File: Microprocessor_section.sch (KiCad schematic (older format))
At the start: 14 parts, among them J15 Conn_01x06_Male, SW1 K2-1102SP-C4SC-04, U5 ESP32-WROOM-32D

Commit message: Start PCB layout
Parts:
- removed SW1: K2-1102SP-C4SC-04, co2_sensor_node:K2-1102SP-xxxC, symbol Switch:SW_MEC_5G
- added SW1: K2-1102SP-C4SC-04, co2_sensor_node:K2-1102SP-xxxC, symbol Switch:SW_Push
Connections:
- net EN: now also SW1.2
- net GND: now also SW1.1
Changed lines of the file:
@@
 Text HLabel 7600 3500 2    50   Output ~ 0
 UART1_TX
-$Comp
-L Switch:SW_MEC_5G SW1
-U 1 1 60A91701
-P 5200 3050
-F 0 "SW1" V 5150 3300 50  0000 R CNN
-F 1 "K2-1102SP-C4SC-04" V 5250 3150 50  0000 L CNN
-F 2 "co2_sensor_node:K2-1102SP-xxxC" H 5200 3250 50  0001 C CNN
-F 3 "https://datasheet.lcsc.com/szlcsc/1811082113_Korean-Hroparts-Elec-K2-1102SP-C4SC-04_C127509.pdf" H 5200 3250 50  0001 C CNN
-F 4 "https://lcsc.com/product-detail/Tactile-Switches_Korean-Hroparts-Elec-K2-1102SP-C4SC-04_C127509.html/?href=jlc-SMT" V 5200 3050 50  0001 C CNN "LCSC"
-	1    5200 3050
-	0    -1   1    0
-$EndComp
 Wire Wire Line
 	5200 2800 5200 2850
@@
 Wire Wire Line
 	2300 4100 2600 4100
+$Comp
+L Switch:SW_Push SW1
+U 1 1 60B19388
+P 5200 3050
+F 0 "SW1" V 5246 3150 50  0000 L CNN
+F 1 "K2-1102SP-C4SC-04" V 5118 3150 50  0000 L CNN
+F 2 "co2_sensor_node:K2-1102SP-xxxC" H 5200 3250 50  0001 C CNN
+F 3 "https://datasheet.lcsc.com/szlcsc/1811082113_Korean-Hroparts-Elec-K2-1102SP-C4SC-04_C127509.pdf" H 5200 3250 50  0001 C CNN
+F 4 "https://lcsc.com/product-detail/Tactile-Switches_Korean-Hroparts-Elec-K2-1102SP-C4SC-04_C127509.html/?href=jlc-SMT" V 5200 3050 50  0001 C CNN "LCSC"
+	1    5200 3050
+	0    -1   -1   0
+$EndComp
 $EndSCHEMATC

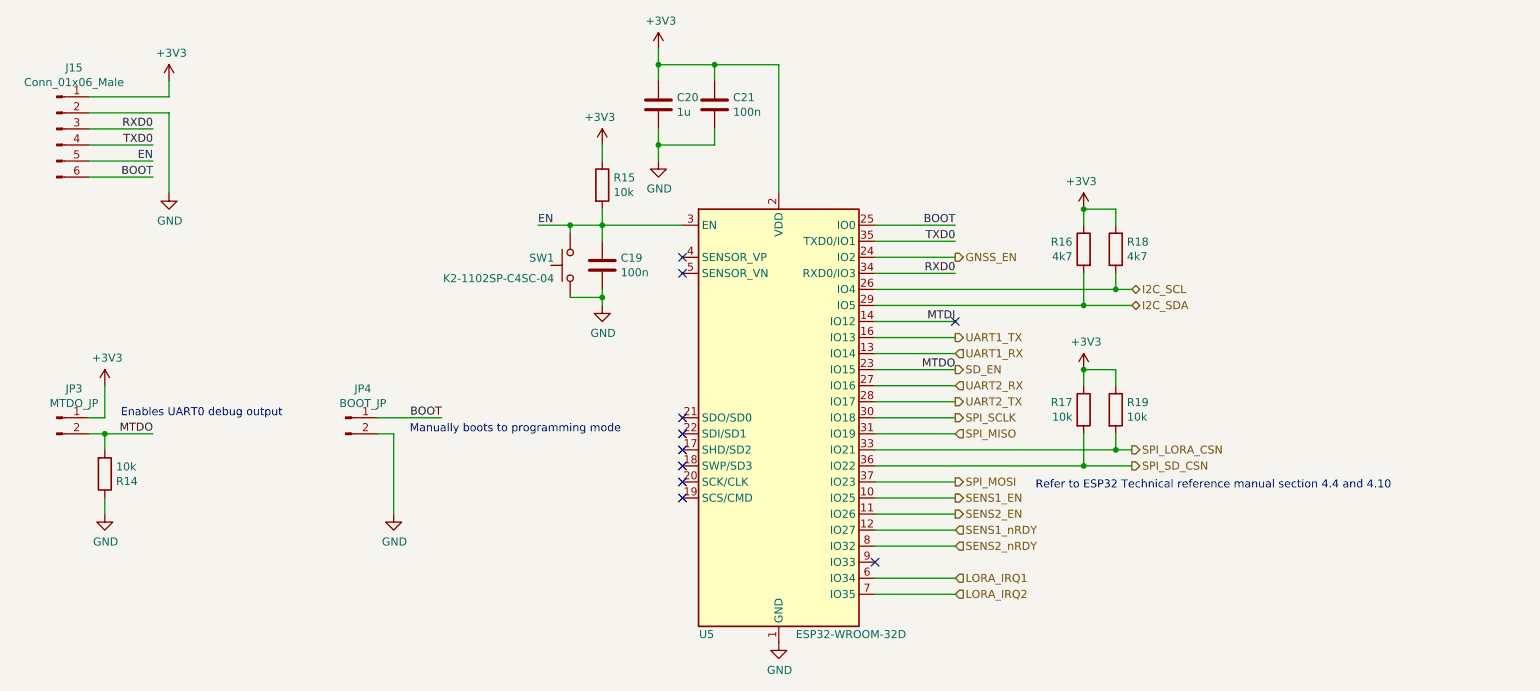
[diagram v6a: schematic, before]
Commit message: First cut at layout
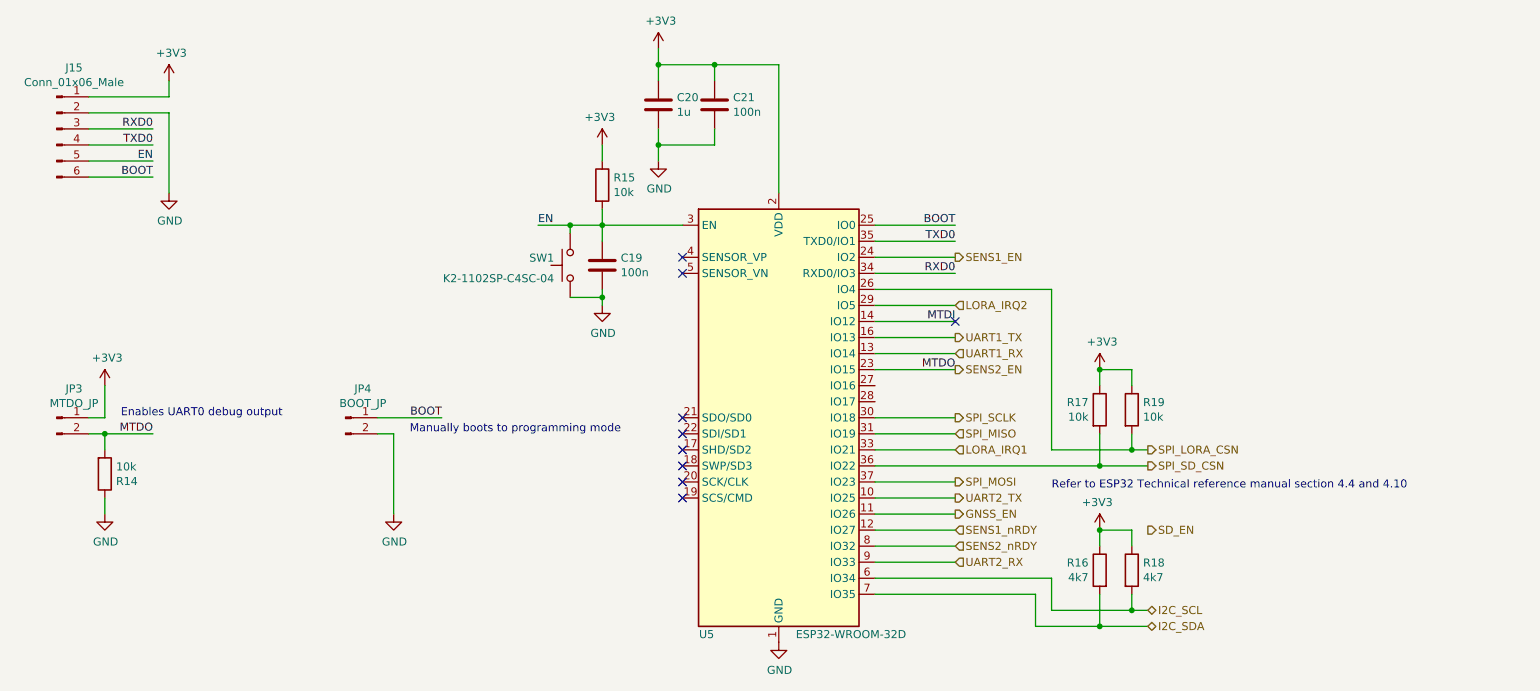
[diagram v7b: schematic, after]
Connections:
- net GNSS_EN: now also U5.11 (IO26); no longer U5.24 (IO2)
- net I2C_SCL: now also U5.6 (IO34); no longer U5.26 (IO4)
- net I2C_SDA: now also U5.7 (IO35); no longer U5.29 (IO5)
- net LORA_IRQ1: now also U5.33 (IO21); no longer U5.6 (IO34)
- net LORA_IRQ2: now also U5.29 (IO5); no longer U5.7 (IO35)
- net SD_EN: no longer JP3.2 (Pin_2), R14.2, U5.23 (IO15)
- net SENS1_EN: now also U5.24 (IO2); no longer U5.10 (IO25)
- net SENS2_EN: now also JP3.2 (Pin_2), R14.2, U5.23 (IO15); no longer U5.11 (IO26)
- net SPI_LORA_CSN: now also U5.26 (IO4); no longer U5.33 (IO21)
- net UART2_RX: now also U5.9 (IO33); no longer U5.27 (IO16)
- net UART2_TX: now also U5.10 (IO25); no longer U5.28 (IO17)
- no-connect marks 10 -> 9
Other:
- moved on the sheet: R16, R17, R18, R19
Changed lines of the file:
@@
 $EndComp
 Wire Wire Line
-	7100 3200 8600 3200
-Wire Wire Line
-	8400 3100 8400 3300
-Wire Wire Line
-	8400 3300 8700 3300
-Connection ~ 8400 3300
-Wire Wire Line
-	7100 3300 8400 3300
-Connection ~ 8400 2700
-Wire Wire Line
-	8600 4200 8700 4200
-Connection ~ 8600 4200
-Wire Wire Line
-	8600 4100 8600 4200
-Wire Wire Line
-	8400 4300 8700 4300
-Connection ~ 8400 4300
-Wire Wire Line
-	8400 4100 8400 4300
-Wire Wire Line
-	7100 4200 8600 4200
-Wire Wire Line
-	7100 4300 8400 4300
-Wire Wire Line
-	8600 3200 8700 3200
-Connection ~ 8600 3200
-Wire Wire Line
-	8400 2700 8600 2700
-Wire Wire Line
-	8400 3700 8600 3700
-Wire Wire Line
-	8600 3700 8600 3800
+	8500 5100 8500 5300
+Wire Wire Line
+	8500 5300 8800 5300
+Connection ~ 8500 4700
+Wire Wire Line
+	8700 4200 8800 4200
+Connection ~ 8700 4200
+Wire Wire Line
+	8700 4100 8700 4200
+Wire Wire Line
+	8500 4300 8800 4300
+Connection ~ 8500 4300
+Wire Wire Line
+	8500 4100 8500 4300
+Wire Wire Line
+	8700 5200 8800 5200
+Wire Wire Line
+	8500 4700 8700 4700
+Wire Wire Line
+	8500 3700 8700 3700
+Wire Wire Line
+	8700 3700 8700 3800
 $Comp
 L power:GND #PWR064
@@
 $EndComp
 Wire Wire Line
-	7100 5100 7600 5100
-Wire Wire Line
-	7100 5000 7600 5000
+	7100 3300 7600 3300
+Wire Wire Line
+	7100 4200 7600 4200
 Wire Wire Line
 	7100 4100 7600 4100
@@
 Text HLabel 7600 4000 2    50   Output ~ 0
 SPI_SCLK
-Text HLabel 7600 3700 2    50   Output ~ 0
+Text HLabel 8800 4700 2    50   Output ~ 0
 SD_EN
-Text HLabel 7600 5100 2    50   Input ~ 0
+Text HLabel 7600 3300 2    50   Input ~ 0
 LORA_IRQ2
-Text HLabel 7600 5000 2    50   Input ~ 0
+Text HLabel 7600 4200 2    50   Input ~ 0
 LORA_IRQ1
-Text HLabel 7600 3000 2    50   Output ~ 0
+Text HLabel 7600 4600 2    50   Output ~ 0
 GNSS_EN
 Text HLabel 7600 4800 2    50   Input ~ 0
 SENS2_nRDY
-Text HLabel 7600 4600 2    50   Output ~ 0
+Text HLabel 7600 3700 2    50   Output ~ 0
 SENS2_EN
 Text HLabel 7600 4700 2    50   Input ~ 0
 SENS1_nRDY
-Text HLabel 7600 4500 2    50   Output ~ 0
+Text HLabel 7600 3000 2    50   Output ~ 0
 SENS1_EN
 Wire Wire Line
@@
 	6100 1800 5750 1800
 Connection ~ 6100 1800
-Connection ~ 8400 3700
-Wire Wire Line
-	8400 3800 8400 3700
+Connection ~ 8500 3700
+Wire Wire Line
+	8500 3800 8500 3700
 $Comp
 L power:+3V3 #PWR066
 U 1 1 60A5A46E
-P 8400 3700
-F 0 "#PWR066" H 8400 3550 50  0001 C CNN
-F 1 "+3V3" H 8415 3873 50  0000 C CNN
-F 2 "" H 8400 3700 50  0001 C CNN
-F 3 "" H 8400 3700 50  0001 C CNN
-	1    8400 3700
+P 8500 3700
+F 0 "#PWR066" H 8500 3550 50  0001 C CNN
+F 1 "+3V3" H 8515 3873 50  0000 C CNN
+F 2 "" H 8500 3700 50  0001 C CNN
+F 3 "" H 8500 3700 50  0001 C CNN
+	1    8500 3700
 	1    0    0    -1
 $EndComp
@@
 L Device:R R19
 U 1 1 60A5A468
-P 8600 3950
-F 0 "R19" H 8670 3996 50  0000 L CNN
-F 1 "10k" H 8670 3905 50  0000 L CNN
-F 2 "Resistor_SMD:R_0603_1608Metric" V 8530 3950 50  0001 C CNN
-F 3 "~" H 8600 3950 50  0001 C CNN
-F 4 "C25804" H 8600 3950 50  0001 C CNN "LCSC"
-	1    8600 3950
+P 8700 3950
+F 0 "R19" H 8770 3996 50  0000 L CNN
+F 1 "10k" H 8770 3905 50  0000 L CNN
+F 2 "Resistor_SMD:R_0603_1608Metric" V 8630 3950 50  0001 C CNN
+F 3 "~" H 8700 3950 50  0001 C CNN
+F 4 "C25804" H 8700 3950 50  0001 C CNN "LCSC"
+	1    8700 3950
 	1    0    0    -1
 $EndComp
@@
 L Device:R R17
 U 1 1 60A5A462
-P 8400 3950
-F 0 "R17" H 8330 3996 50  0000 R CNN
-F 1 "10k" H 8330 3905 50  0000 R CNN
-F 2 "Resistor_SMD:R_0603_1608Metric" V 8330 3950 50  0001 C CNN
-F 3 "~" H 8400 3950 50  0001 C CNN
-F 4 "C25804" H 8400 3950 50  0001 C CNN "LCSC"
-	1    8400 3950
-	1    0    0    -1
-$EndComp
-Wire Wire Line
-	8400 2800 8400 2700
-Wire Wire Line
-	8600 2800 8600 2700
-Wire Wire Line
-	8600 3200 8600 3100
+P 8500 3950
+F 0 "R17" H 8430 3996 50  0000 R CNN
+F 1 "10k" H 8430 3905 50  0000 R CNN
+F 2 "Resistor_SMD:R_0603_1608Metric" V 8430 3950 50  0001 C CNN
+F 3 "~" H 8500 3950 50  0001 C CNN
+F 4 "C25804" H 8500 3950 50  0001 C CNN "LCSC"
+	1    8500 3950
+	1    0    0    -1
+$EndComp
+Wire Wire Line
+	8500 4800 8500 4700
+Wire Wire Line
+	8700 4800 8700 4700
+Wire Wire Line
+	8700 5200 8700 5100
 $Comp
 L power:+3V3 #PWR065
 U 1 1 60A5400B
-P 8400 2700
-F 0 "#PWR065" H 8400 2550 50  0001 C CNN
-F 1 "+3V3" H 8415 2873 50  0000 C CNN
-F 2 "" H 8400 2700 50  0001 C CNN
-F 3 "" H 8400 2700 50  0001 C CNN
-	1    8400 2700
+P 8500 4700
+F 0 "#PWR065" H 8500 4550 50  0001 C CNN
+F 1 "+3V3" H 8515 4873 50  0000 C CNN
+F 2 "" H 8500 4700 50  0001 C CNN
+F 3 "" H 8500 4700 50  0001 C CNN
+	1    8500 4700
 	-1   0    0    -1
 $EndComp
@@
 L Device:R R16
 U 1 1 60A50D69
-P 8400 2950
-F 0 "R16" H 8470 2996 50  0000 L CNN
-F 1 "4k7" H 8470 2905 50  0000 L CNN
-F 2 "Resistor_SMD:R_0603_1608Metric" V 8330 2950 50  0001 C CNN
-F 3 "~" H 8400 2950 50  0001 C CNN
-F 4 "C23162" H 8400 2950 50  0001 C CNN "LCSC"
-	1    8400 2950
+P 8500 4950
+F 0 "R16" H 8570 4996 50  0000 L CNN
+F 1 "4k7" H 8570 4905 50  0000 L CNN
+F 2 "Resistor_SMD:R_0603_1608Metric" V 8430 4950 50  0001 C CNN
+F 3 "~" H 8500 4950 50  0001 C CNN
+F 4 "C23162" H 8500 4950 50  0001 C CNN "LCSC"
+	1    8500 4950
 	-1   0    0    -1
 $EndComp
@@
 L Device:R R18
 U 1 1 60A501AF
-P 8600 2950
-F 0 "R18" H 8670 2996 50  0000 L CNN
-F 1 "4k7" H 8670 2905 50  0000 L CNN
-F 2 "Resistor_SMD:R_0603_1608Metric" V 8530 2950 50  0001 C CNN
-F 3 "~" H 8600 2950 50  0001 C CNN
-F 4 "C23162" H 8600 2950 50  0001 C CNN "LCSC"
-	1    8600 2950
+P 8700 4950
+F 0 "R18" H 8770 4996 50  0000 L CNN
+F 1 "4k7" H 8770 4905 50  0000 L CNN
+F 2 "Resistor_SMD:R_0603_1608Metric" V 8630 4950 50  0001 C CNN
+F 3 "~" H 8700 4950 50  0001 C CNN
+F 4 "C23162" H 8700 4950 50  0001 C CNN "LCSC"
+	1    8700 4950
 	1    0    0    -1
 $EndComp
@@
 Wire Wire Line
 	7600 3600 7100 3600
-Text HLabel 8700 4300 2    50   Output ~ 0
+Text HLabel 8800 4300 2    50   Output ~ 0
 SPI_SD_CSN
-Text HLabel 8700 4200 2    50   Output ~ 0
+Text HLabel 8800 4200 2    50   Output ~ 0
 SPI_LORA_CSN
-Text HLabel 8700 3300 2    50   BiDi ~ 0
+Text HLabel 8800 5300 2    50   BiDi ~ 0
 I2C_SDA
-Text HLabel 8700 3200 2    50   BiDi ~ 0
+Text HLabel 8800 5200 2    50   BiDi ~ 0
 I2C_SCL
 Text HLabel 7600 3600 2    50   Input ~ 0
@@
 	4100 4100 4100 4600
 Wire Wire Line
-	7100 3900 7600 3900
-Wire Wire Line
-	7600 3800 7100 3800
-Text HLabel 7600 3800 2    50   Input ~ 0
+	7100 4500 7600 4500
+Wire Wire Line
+	7600 4900 7100 4900
+Text HLabel 7600 4900 2    50   Input ~ 0
 UART2_RX
-Text HLabel 7600 3900 2    50   Output ~ 0
+Text HLabel 7600 4500 2    50   Output ~ 0
 UART2_TX
-Wire Wire Line
-	7600 4500 7100 4500
-Text Notes 8100 4450 0    50   ~ 0
+Text Notes 8200 4450 0    50   ~ 0
 Refer to ESP32 Technical reference manual section 4.4 and 4.10\n
 NoConn ~ 7600 3400
-NoConn ~ 7100 4900
 Wire Wire Line
 	2300 4100 2300 4200
@@
 	0    -1   -1   0
 $EndComp
+Connection ~ 8700 5200
+Connection ~ 8500 5300
+Wire Wire Line
+	7100 4300 8500 4300
+Wire Wire Line
+	7100 3200 8200 3200
+Wire Wire Line
+	8200 3200 8200 4200
+Wire Wire Line
+	8200 4200 8700 4200
+Wire Wire Line
+	8200 5200 8700 5200
+Wire Wire Line
+	8100 5300 8500 5300
+Wire Wire Line
+	7100 5000 8200 5000
+Wire Wire Line
+	8200 5000 8200 5200
+Wire Wire Line
+	8100 5300 8100 5100
+Wire Wire Line
+	8100 5100 7100 5100
 $EndSCHEMATC

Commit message: Layout complete, barring review and polish
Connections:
- net +3V3: now also JP3.2 (Pin_2); no longer JP3.1 (Pin_1)
- net I2C_SCL: now also R16.2, U5.7 (IO35); no longer R18.2, U5.6 (IO34)
- net I2C_SDA: now also R18.2, U5.6 (IO34); no longer R16.2, U5.7 (IO35)
- net LORA_IRQ1: now also U5.29 (IO5); no longer U5.33 (IO21)
- net LORA_IRQ2: now also U5.33 (IO21); no longer U5.29 (IO5)
- net SENS2_EN: now also JP3.1 (Pin_1); no longer JP3.2 (Pin_2)
- net UART2_RX: now also U5.10 (IO25); no longer U5.9 (IO33)
- net UART2_TX: now also U5.9 (IO33); no longer U5.10 (IO25)
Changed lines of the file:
@@
 $EndComp
+Wire Wire Line
+	7100 4200 7600 4200
 Wire Wire Line
 	7100 3300 7600 3300
-Wire Wire Line
-	7100 4200 7600 4200
 Wire Wire Line
 	7100 4100 7600 4100
@@
 Text HLabel 8800 4700 2    50   Output ~ 0
 SD_EN
+Text HLabel 7600 4200 2    50   Input ~ 0
+LORA_IRQ2
 Text HLabel 7600 3300 2    50   Input ~ 0
-LORA_IRQ2
-Text HLabel 7600 4200 2    50   Input ~ 0
 LORA_IRQ1
 Text HLabel 7600 4600 2    50   Output ~ 0
@@
 Text HLabel 8800 4200 2    50   Output ~ 0
 SPI_LORA_CSN
+Text HLabel 8800 5200 2    50   BiDi ~ 0
+I2C_SDA
 Text HLabel 8800 5300 2    50   BiDi ~ 0
-I2C_SDA
-Text HLabel 8800 5200 2    50   BiDi ~ 0
 I2C_SCL
 Text HLabel 7600 3600 2    50   Input ~ 0
@@
 L Connector:Conn_01x02_Male JP3
 U 1 1 60AA0F54
-P 2000 4000
-F 0 "JP3" H 2108 4181 50  0000 C CNN
-F 1 "MTDO_JP" H 2108 4090 50  0000 C CNN
-F 2 "Connector_PinHeader_2.54mm:PinHeader_1x02_P2.54mm_Vertical" H 2000 4000 50  0001 C CNN
-F 3 "~" H 2000 4000 50  0001 C CNN
-	1    2000 4000
-	1    0    0    -1
+P 2000 4100
+F 0 "JP3" H 2100 3800 50  0000 C CNN
+F 1 "MTDO_JP" H 2100 3900 50  0000 C CNN
+F 2 "Connector_PinHeader_2.54mm:PinHeader_1x02_P2.54mm_Vertical" H 2000 4100 50  0001 C CNN
+F 3 "~" H 2000 4100 50  0001 C CNN
+	1    2000 4100
+	1    0    0    1
 $EndComp
 Wire Wire Line
@@
 	4100 4100 4100 4600
 Wire Wire Line
-	7100 4500 7600 4500
-Wire Wire Line
-	7600 4900 7100 4900
-Text HLabel 7600 4900 2    50   Input ~ 0
+	7100 4900 7600 4900
+Wire Wire Line
+	7600 4500 7100 4500
+Text HLabel 7600 4500 2    50   Input ~ 0
 UART2_RX
-Text HLabel 7600 4500 2    50   Output ~ 0
+Text HLabel 7600 4900 2    50   Output ~ 0
 UART2_TX
 Text Notes 8200 4450 0    50   ~ 0
